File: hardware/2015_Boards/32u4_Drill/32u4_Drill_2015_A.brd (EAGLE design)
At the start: 31.8 x 55.9 mm, 26 parts, among them U2 XBEE-1B3

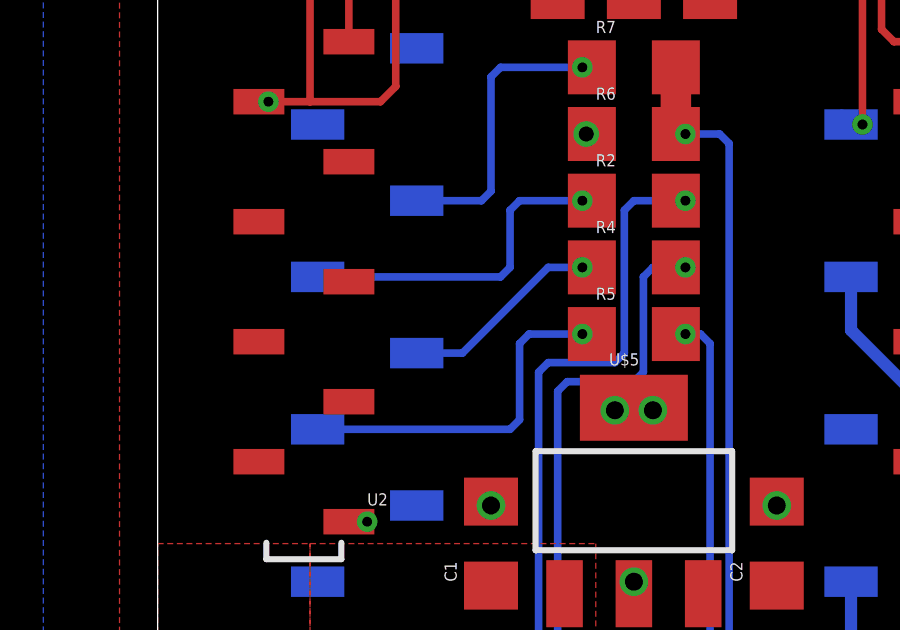
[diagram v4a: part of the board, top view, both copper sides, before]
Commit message: Cleaned up traces
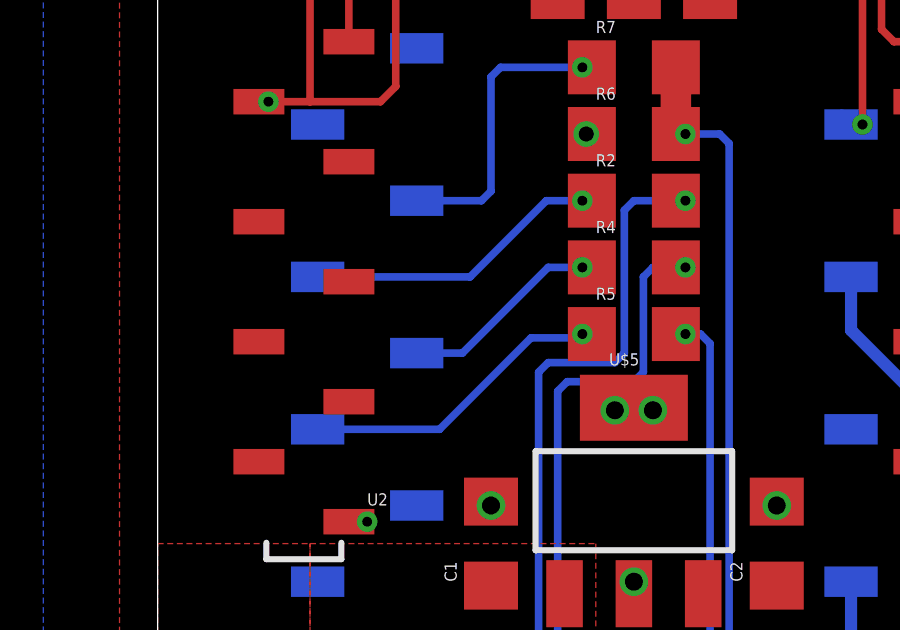
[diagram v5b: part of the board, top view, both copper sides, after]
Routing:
- net INH: track 12.1 -> 10.6 mm
- net IN1: track 11.4 -> 10.3 mm
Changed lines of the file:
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@@
 <contactref element="R2" pad="1"/>
 <contactref element="U$1" pad="P$28"/>
-<wire x1="5.334" y1="36.83" x2="11.43" y2="36.83" width="0.254" layer="16"/>
-<wire x1="11.43" y1="36.83" x2="11.7475" y2="37.1475" width="0.254" layer="16"/>
-<wire x1="11.7475" y1="37.1475" x2="11.7475" y2="39.0525" width="0.254" layer="16"/>
-<wire x1="11.7475" y1="39.0525" x2="12.065" y2="39.37" width="0.254" layer="16"/>
-<wire x1="12.065" y1="39.37" x2="14.1575" y2="39.37" width="0.254" layer="16"/>
 <via x="14.1575" y="39.37" extent="1-16" drill="0.3302"/>
 <wire x1="14.605" y1="39.37" x2="14.475" y2="39.37" width="0.254" layer="1"/>
 <wire x1="14.475" y1="39.37" x2="14.1575" y2="39.37" width="0.4064" layer="1"/>
+<wire x1="5.334" y1="36.83" x2="10.414" y2="36.83" width="0.254" layer="16"/>
+<wire x1="10.414" y1="36.83" x2="12.954" y2="39.37" width="0.254" layer="16"/>
+<wire x1="12.954" y1="39.37" x2="14.1575" y2="39.37" width="0.254" layer="16"/>
 </signal>
 <signal name="IN2">
@@
 <contactref element="R5" pad="1"/>
 <contactref element="U$1" pad="P$26"/>
-<wire x1="5.334" y1="31.75" x2="11.7475" y2="31.75" width="0.254" layer="16"/>
-<wire x1="11.7475" y1="31.75" x2="12.065" y2="32.0675" width="0.254" layer="16"/>
-<wire x1="12.065" y1="32.0675" x2="12.065" y2="34.6075" width="0.254" layer="16"/>
-<wire x1="12.065" y1="34.6075" x2="12.3825" y2="34.925" width="0.254" layer="16"/>
-<wire x1="12.3825" y1="34.925" x2="14.1575" y2="34.925" width="0.254" layer="16"/>
 <via x="14.1575" y="34.925" extent="1-16" drill="0.3302"/>
 <wire x1="14.605" y1="34.925" x2="14.475" y2="34.925" width="0.254" layer="1"/>
 <wire x1="14.475" y1="34.925" x2="14.1575" y2="34.925" width="0.4064" layer="1"/>
+<wire x1="5.334" y1="31.75" x2="9.398" y2="31.75" width="0.254" layer="16"/>
+<wire x1="9.398" y1="31.75" x2="12.446" y2="34.798" width="0.254" layer="16"/>
+<wire x1="12.446" y1="34.798" x2="14.0305" y2="34.798" width="0.254" layer="16"/>
+<wire x1="14.0305" y1="34.798" x2="14.1575" y2="34.925" width="0.254" layer="16"/>
 </signal>
 <signal name="N$6">

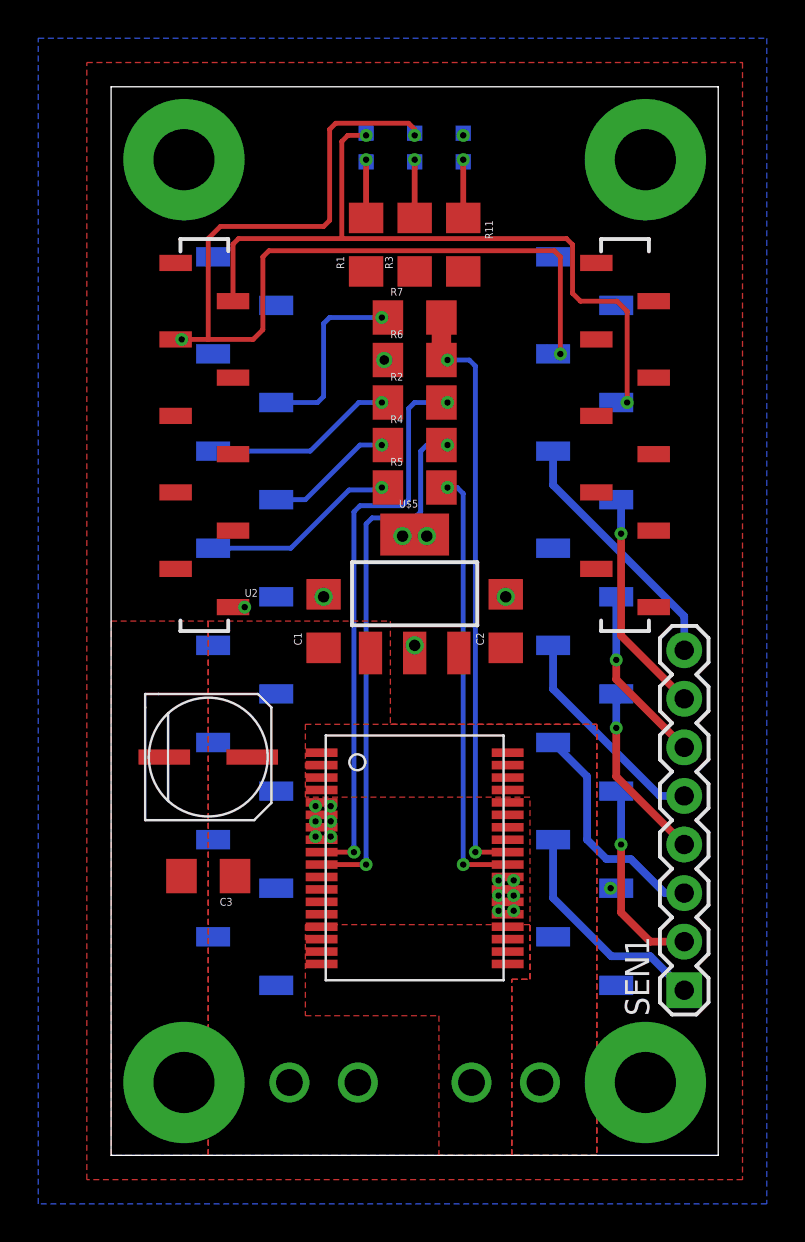
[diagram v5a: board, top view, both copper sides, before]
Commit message: Fixed a schematic connection issue
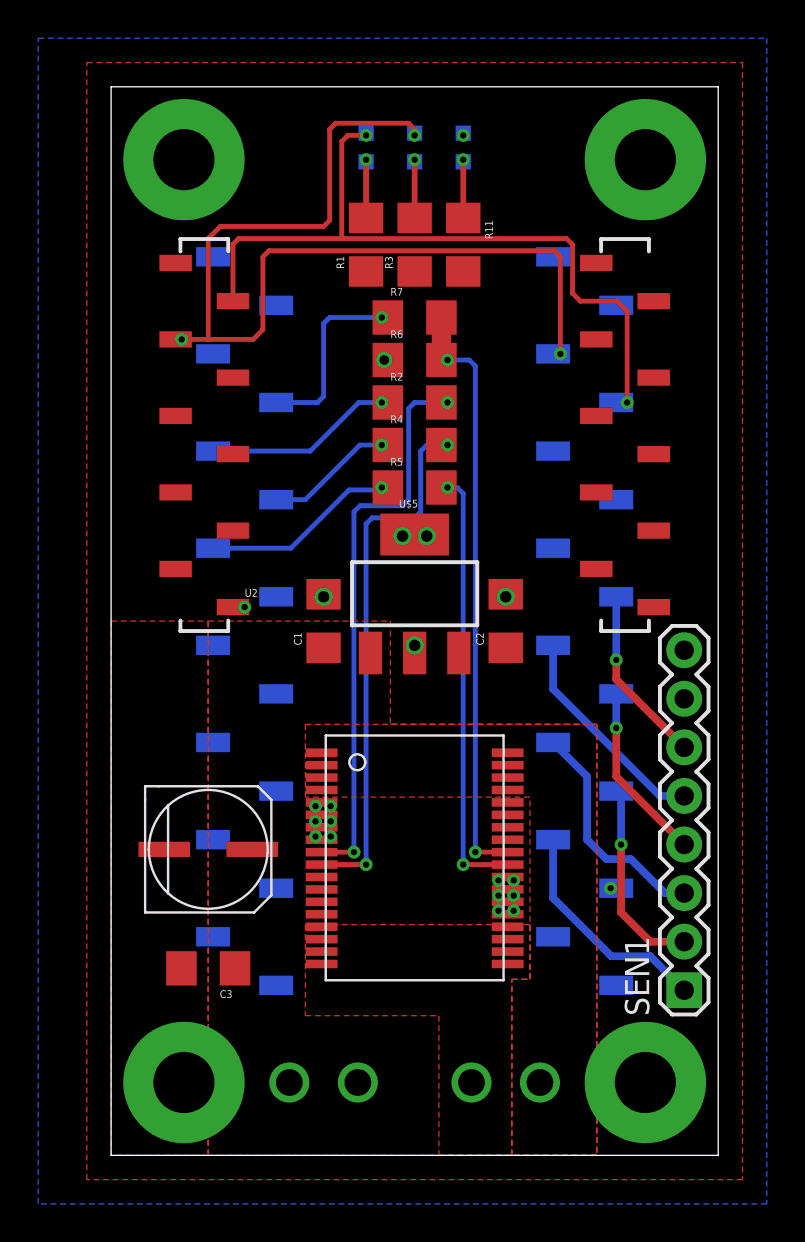
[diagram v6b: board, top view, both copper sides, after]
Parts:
- moved C3 4.83 mm to (5.08, 9.78)
- moved U$6 4.83 mm to (5.08, 16.0)
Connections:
- removed net N$13: SEN1.7, U$1.P$11
- net 3.3V: now also SEN1.8
- net GND: now also U$6.NEG
- net N$14: now also SEN1.7; no longer SEN1.8, U$1.P$12
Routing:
- net N$14: track 13.3 -> 0.00 mm
- net N$13: track 11.9 -> 0.00 mm, vias 1 -> 0
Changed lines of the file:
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@@
 <element name="R6" library="SparkFun-Passives" package="1206" value="1k" x="15.875" y="41.5925"/>
 <element name="R7" library="SparkFun-Passives" package="1206" value="" x="15.875" y="43.815"/>
-<element name="C3" library="SparkFun-Passives" package="1206" value="0.1uF" x="5.08" y="14.605" rot="R180"/>
-<element name="U$6" library="New" package="ELECTRO-CAP" value="100UF-ELECTRO-CAP" x="5.08" y="20.828"/>
+<element name="C3" library="SparkFun-Passives" package="1206" value="0.1uF" x="5.08" y="9.779" rot="R180"/>
 <element name="SEN1" library="SparkFun-Connectors" package="1X08" value="" x="29.972" y="8.636" rot="R90"/>
+<element name="U$6" library="New" package="ELECTRO-CAP" value="100UF-ELECTRO-CAP" x="5.08" y="16.002"/>
 </elements>
 <signals>
@@
 <wire x1="20.6375" y1="29.34" x2="20.6375" y2="29.21" width="0.6096" layer="1"/>
 <contactref element="R6" pad="1"/>
-<contactref element="C3" pad="2"/>
 <polygon width="0.3048" layer="1">
 <vertex x="0" y="0"/>
@@
 <via x="14.2875" y="41.5925" extent="1-16" drill="0.5" shape="square"/>
 <wire x1="14.2875" y1="41.5925" x2="14.475" y2="41.5925" width="0.254" layer="1"/>
+<contactref element="C3" pad="2"/>
+<contactref element="U$6" pad="NEG"/>
 </signal>
 <signal name="RESET">
@@
 <wire x1="26.1239" y1="13.97" x2="26.416" y2="13.97" width="0.3048" layer="16"/>
 <contactref element="C2" pad="1"/>
+<contactref element="SEN1" pad="8"/>
 </signal>
 <signal name="DIO4">
@@
 <wire x1="26.416" y1="25.908" x2="26.416" y2="29.21" width="0.4064" layer="16"/>
 </signal>
-<signal name="N$13">
-<contactref element="U$1" pad="P$11"/>
+<signal name="N$14">
 <contactref element="SEN1" pad="7"/>
-<wire x1="29.972" y1="23.876" x2="26.67" y2="27.178" width="0.4064" layer="1"/>
-<wire x1="26.67" y1="27.178" x2="26.67" y2="32.512" width="0.4064" layer="1"/>
-<via x="26.67" y="32.512" extent="1-16" drill="0.3302"/>
-<wire x1="26.67" y1="32.512" x2="26.67" y2="34.036" width="0.4064" layer="16"/>
-<wire x1="26.67" y1="34.036" x2="26.416" y2="34.29" width="0.4064" layer="16"/>
-</signal>
-<signal name="N$14">
-<contactref element="U$1" pad="P$12"/>
-<contactref element="SEN1" pad="8"/>
-<wire x1="29.972" y1="26.416" x2="29.972" y2="28.194" width="0.4064" layer="16"/>
-<wire x1="29.972" y1="28.194" x2="23.114" y2="35.052" width="0.4064" layer="16"/>
-<wire x1="23.114" y1="35.052" x2="23.114" y2="36.83" width="0.4064" layer="16"/>
 </signal>
 </signals>
